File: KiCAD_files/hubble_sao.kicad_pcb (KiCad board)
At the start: 2 copper layers, 38 x 45.5 mm, 41 parts, among them J1 Conn_02x03_Counter_Clockwise, J2 Conn_02x03_Odd_Even, Q1 DMP3099L-7, SW1 SW_Push_Shielded, U1 VEML3328, U2 LSM6DSO, U3 ATmega328PB-A, U4 TLV9062xD, U5 TLV9062xD

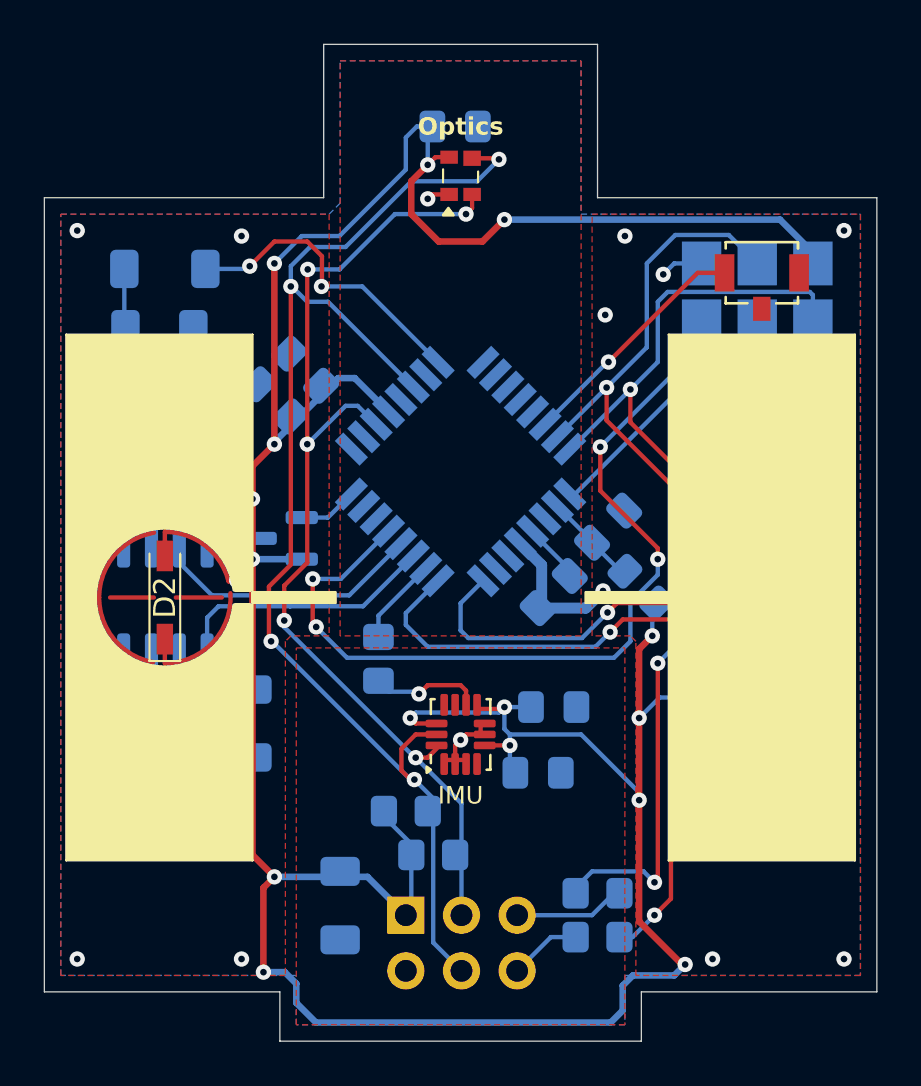
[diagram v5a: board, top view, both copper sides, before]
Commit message: Merged the front copper pours in a single ground plane
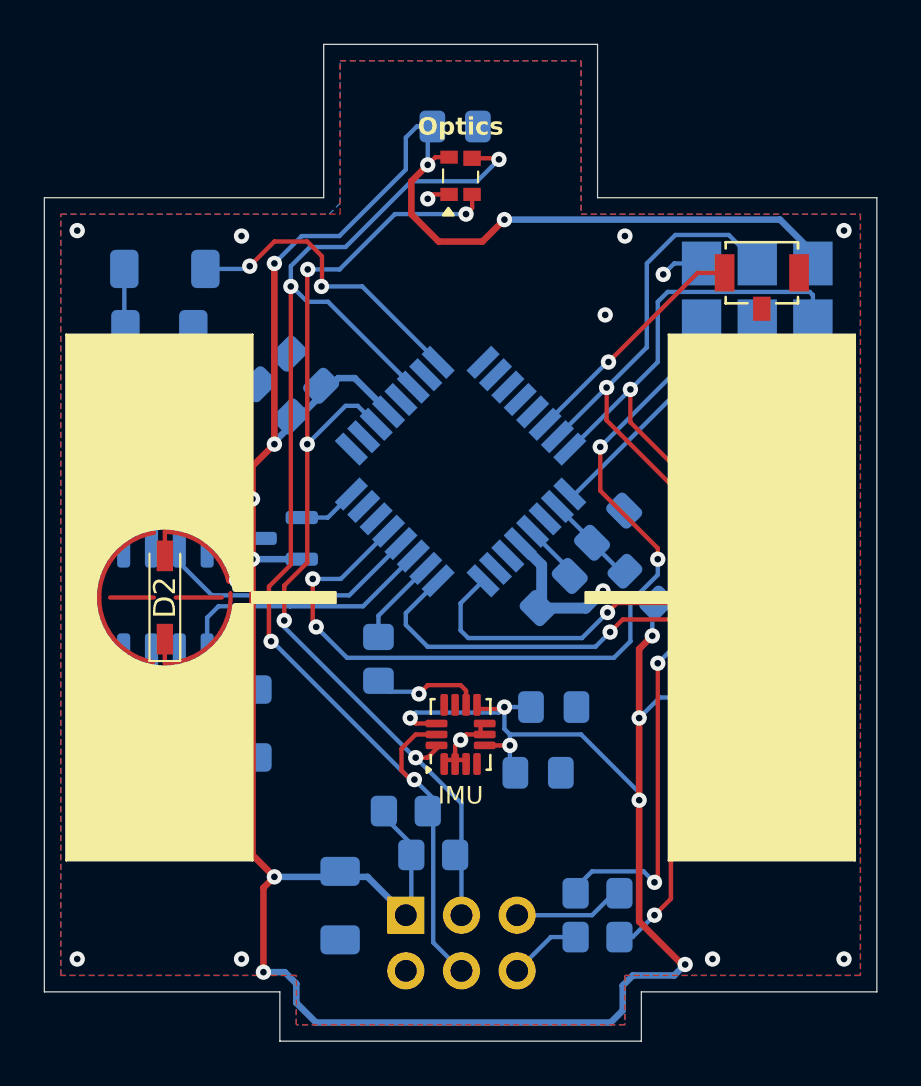
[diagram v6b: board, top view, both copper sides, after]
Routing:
- removed copper zone on F.Cu, net (none)
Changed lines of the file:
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@@
 		(tags "resistor handsolder")
 		(property "Reference" "R1"
-			(at -3.3 0 360)
+			(at -3.3 0 0)
 			(layer "B.SilkS")
 			(effects
@@
 		)
 		(property "Value" "220"
-			(at 0 -1.82 360)
+			(at 0 -1.82 0)
 			(layer "B.Fab")
 			(effects
@@
 		)
 		(fp_text user "${REFERENCE}"
-			(at -3.3 0 360)
+			(at -3.3 0 0)
 			(layer "B.Fab")
 			(effects
@@
 		(tags "diode reverse")
 		(property "Reference" "D6"
-			(at 3.75 -0.25 360)
+			(at 3.75 -0.25 0)
 			(layer "B.SilkS")
 			(effects
@@
 		)
 		(property "Value" "LED"
-			(at 0 -2.145 360)
+			(at 0 -2.145 0)
 			(layer "B.Fab")
 			(effects
@@
 		)
 		(fp_text user "${REFERENCE}"
-			(at 0 0 360)
+			(at 0 0 0)
 			(layer "B.Fab")
 			(effects
@@
 	)
 	(zone
-		(net 0)
-		(net_name "")
-		(layer "F.Cu")
-		(name "Body_panel_1")
-		(hatch edge 0.5)
-		(priority 1)
-		(connect_pads
-			(clearance 0.5)
-		)
-		(min_thickness 0.25)
-		(filled_areas_thickness no)
-		(fill yes
-			(thermal_gap 0.5)
-			(thermal_bridge_width 0.5)
-			(island_removal_mode 1)
-			(island_area_min 10)
-		)
-		(polygon
-			(pts
-				(xy 84.5 100) (xy 95.5 100) (xy 95.5 126.25) (xy 84.5 126.25)
-			)
-		)
-	)
-	(zone
-		(net 20)
-		(net_name "GND")
-		(layer "F.Cu")
-		(name "Optics_cutout")
-		(hatch edge 0.5)
-		(priority 3)
-		(connect_pads
-			(clearance 0)
-		)
-		(min_thickness 0.25)
-		(filled_areas_thickness no)
-		(fill yes
-			(thermal_gap 0.5)
-			(thermal_bridge_width 0.5)
-			(smoothing fillet)
-			(radius 0.5)
-		)
-		(polygon
-			(pts
-				(xy 71.75 107) (xy 84 107) (xy 84 126.25) (xy 82.25 126.25) (xy 82 126.5) (xy 82 141.75) (xy 71.75 141.75)
-			)
-		)
-	)
-	(zone
 		(net 20)
 		(net_name "GND")
 		(layer "F.Cu")
-		(name "Optics_cutout")
-		(hatch edge 0.5)
-		(connect_pads
-			(clearance 0)
-		)
-		(min_thickness 0.25)
-		(filled_areas_thickness no)
-		(fill yes
-			(thermal_gap 0.5)
-			(thermal_bridge_width 0.5)
-			(smoothing fillet)
-			(radius 0.5)
-		)
-		(polygon
-			(pts
-				(xy 96 107) (xy 108.25 107) (xy 108.25 141.75) (xy 98 141.75) (xy 98 126.5) (xy 97.75 126.25) (xy 96 126.25)
-			)
-		)
-	)
-	(zone
-		(net 0)
-		(net_name "")
-		(layer "F.Cu")
-		(name "Body_panel_2")
 		(hatch edge 0.5)
-		(priority 1)
 		(connect_pads
-			(clearance 0.5)
+			(clearance 0.25)
 		)
 		(min_thickness 0.25)
@@
 			(thermal_gap 0.5)
 			(thermal_bridge_width 0.5)
-			(island_removal_mode 1)
-			(island_area_min 10)
 		)
 		(polygon
 			(pts
-				(xy 82.5 126.8) (xy 97.5 126.8) (xy 97.5 144) (xy 82.5 144)
+				(xy 71.75 107) (xy 84.5 107) (xy 84.5 100) (xy 95.5 100) (xy 95.5 107) (xy 108.25 107) (xy 108.25 141.75)
+				(xy 97.5 141.75) (xy 97.5 144) (xy 82.5 144) (xy 82.5 141.75) (xy 71.75 141.75)
 			)
 		)

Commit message: Replaced some 1206 resistors by 0805s to tighten up the PCB
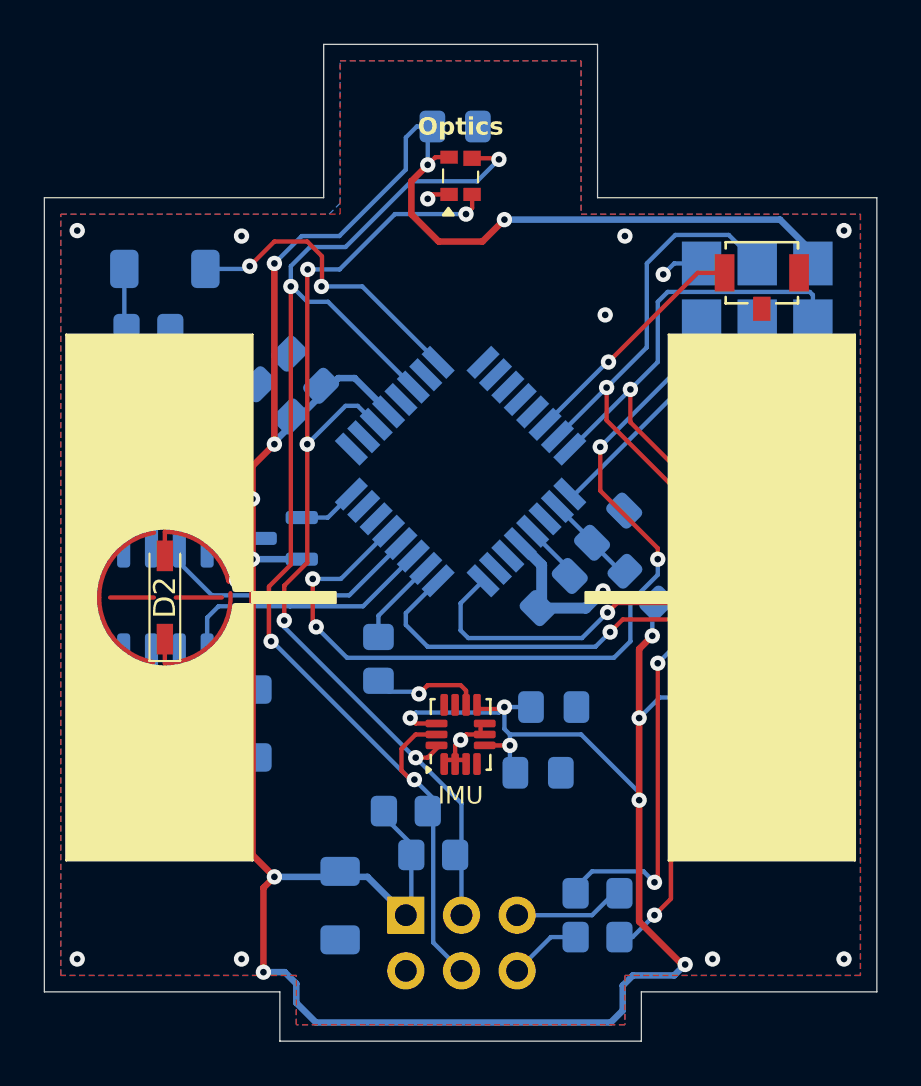
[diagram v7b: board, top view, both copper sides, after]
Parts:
- R1, R10, R3, R4, R5: footprint Resistor_SMD:R_1206_3216Metric_Pad1.30x1.75mm_HandSolder -> Resistor_SMD:R_0805_2012Metric_Pad1.20x1.40mm_HandSolder
- moved C10 1.90 mm to (77.2, 130.2)
- moved R10 1.77 mm to (77.2, 132.2)
- moved R3 1.52 mm to (103.8, 117.0)
- moved R5 1.52 mm to (75.8, 117.0)
- moved R4 1.37 mm to (104.5, 132.2)
- moved C14 1.27 mm to (75.8, 119.2)
- moved C8 1.25 mm to (103.8, 119.0)
- moved C9 1.00 mm to (104.5, 130.0)
- moved R1 0.50 mm to (75.8, 112.2)
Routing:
- net Net-(D1-K): track 11.6 -> 8.46 mm
- net Net-(D3-K): track 12.1 -> 8.91 mm
- net Net-(D5-K): track 10.8 -> 7.87 mm
- net Net-(D4-K): track 12.0 -> 9.09 mm
- net /PANEL3: track 25.2 -> 23.0 mm
- net /PANEL2: track 19.0 -> 17.0 mm
- net /PANEL4: track 27.6 -> 26.0 mm
- net /PANEL1: track 19.0 -> 17.5 mm

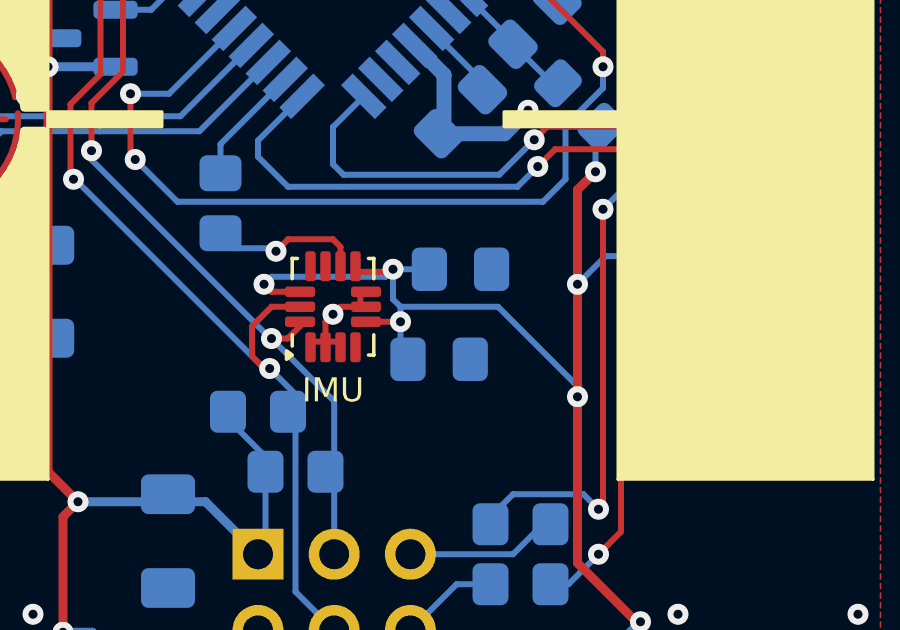
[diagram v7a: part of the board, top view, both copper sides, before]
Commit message: Cleaned up the PCB around the IMU
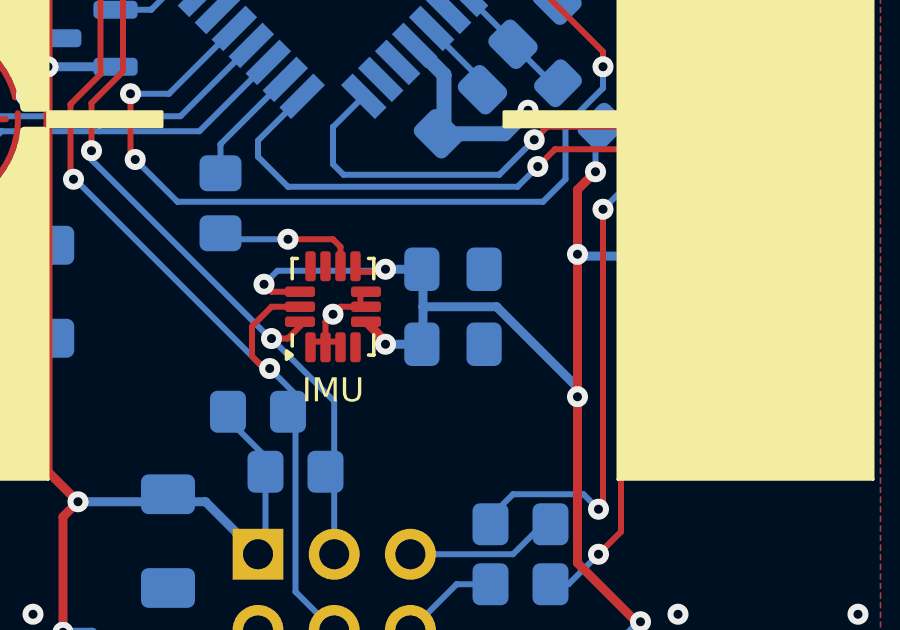
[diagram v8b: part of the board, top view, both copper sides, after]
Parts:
- moved C3 0.68 mm to (94.0, 132.0)
- moved C5 0.25 mm to (94.0, 129.5)
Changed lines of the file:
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@@
 	(footprint "Capacitor_SMD:C_0805_2012Metric_Pad1.18x1.45mm_HandSolder"
 		(layer "B.Cu")
-		(at 93.5375 132.5)
+		(at 94 132)
 		(descr "Capacitor SMD 0805 (2012 Metric), square (rectangular) end terminal, IPC_7351 nominal with elongated pad for handsoldering. (Body size source: IPC-SM-782 page 76, https://www.pcb-3d.com/wordpress/wp-content/uploads/ipc-sm-782a_amendment_1_and_2.pdf, https://docs.google.com/spreadsheets/d/1BsfQQcO9C6DZCsRaXUlFlo91Tg2WpOkGARC1WS5S8t0/edit?usp=sharing), generated with kicad-footprint-generator")
 		(tags "capacitor handsolder")
@@
 	(footprint "Capacitor_SMD:C_0805_2012Metric_Pad1.18x1.45mm_HandSolder"
 		(layer "B.Cu")
-		(at 94.25 129.5)
+		(at 94 129.5)
 		(descr "Capacitor SMD 0805 (2012 Metric), square (rectangular) end terminal, IPC_7351 nominal with elongated pad for handsoldering. (Body size source: IPC-SM-782 page 76, https://www.pcb-3d.com/wordpress/wp-content/uploads/ipc-sm-782a_amendment_1_and_2.pdf, https://docs.google.com/spreadsheets/d/1BsfQQcO9C6DZCsRaXUlFlo91Tg2WpOkGARC1WS5S8t0/edit?usp=sharing), generated with kicad-footprint-generator")
 		(tags "capacitor handsolder")
@@
 	)
 	(segment
-		(start 92.25 131.25)
-		(end 91.1 131.25)
-		(width 0.2)
-		(layer "F.Cu")
-		(net 18)
-	)
-	(segment
 		(start 81.5 137.25)
 		(end 80.5 136.25)
@@
 	)
 	(segment
-		(start 92 129.5)
-		(end 91.9125 129.5875)
-		(width 0.2)
-		(layer "F.Cu")
-		(net 18)
-	)
-	(segment
 		(start 81 137.75)
 		(end 81.5 137.25)
@@
 	)
 	(segment
-		(start 87.75 105.5)
-		(end 88.5 104.75)
+		(start 91.75 132)
+		(end 91.75 131.9)
 		(width 0.3)
 		(layer "F.Cu")
@@
 	)
 	(segment
-		(start 91.9125 129.5875)
-		(end 90.75 129.5875)
-		(width 0.2)
+		(start 91.75 131.9)
+		(end 91.1 131.25)
+		(width 0.3)
+		(layer "F.Cu")
+		(net 18)
+	)
+	(segment
+		(start 87.75 105.5)
+		(end 88.5 104.75)
+		(width 0.3)
 		(layer "F.Cu")
 		(net 18)
@@
 	)
 	(segment
+		(start 91.75 129.5)
+		(end 91.6625 129.5875)
+		(width 0.2)
+		(layer "F.Cu")
+		(net 18)
+	)
+	(segment
 		(start 87.75 107)
 		(end 87.75 105.5)
@@
 	)
 	(segment
+		(start 91.6625 129.5875)
+		(end 90.75 129.5875)
+		(width 0.2)
+		(layer "F.Cu")
+		(net 18)
+	)
+	(segment
 		(start 80.5 118.5)
 		(end 81.5 117.5)
@@
 	)
 	(via
-		(at 92.25 131.25)
-		(size 0.7)
-		(drill 0.3)
-		(layers "F.Cu" "B.Cu")
-		(net 18)
-	)
-	(via
 		(at 80.5 122.75)
 		(size 0.7)
@@
 	)
 	(via
-		(at 98.15 130)
+		(at 98.15 129)
 		(size 0.7)
 		(drill 0.3)
@@
 	)
 	(via
-		(at 92 129.5)
+		(at 91.75 129.5)
 		(size 0.7)
 		(drill 0.3)
@@
 		(net 18)
 	)
-	(segment
-		(start 92.25 131.25)
-		(end 92.25 132)
-		(width 0.2)
-		(layer "B.Cu")
+	(via
+		(at 91.75 132)
+		(size 0.7)
+		(drill 0.3)
+		(layers "F.Cu" "B.Cu")
 		(net 18)
 	)
@@
 	)
 	(segment
+		(start 93 130.75)
+		(end 93 129.5375)
+		(width 0.3)
+		(layer "B.Cu")
+		(net 18)
+	)
+	(segment
 		(start 81.5 117.401471)
 		(end 84.417848 114.483623)
@@
 	)
 	(segment
+		(start 92.6375 129.575)
+		(end 92.7125 129.5)
+		(width 0.2)
+		(layer "B.Cu")
+		(net 18)
+	)
+	(segment
 		(start 87.5 103.5)
 		(end 88 103)
@@
 	)
 	(segment
-		(start 98.15 133.75)
-		(end 98.15 133.4)
+		(start 91.7 129.55)
+		(end 88.15 129.55)
 		(width 0.2)
 		(layer "B.Cu")
@@
 	)
 	(segment
-		(start 99.0875 129.0625)
-		(end 101.5 129.0625)
-		(width 0.2)
+		(start 93 130.75)
+		(end 93 131.9625)
+		(width 0.3)
 		(layer "B.Cu")
 		(net 18)
@@
 	)
 	(segment
+		(start 88.15 129.55)
+		(end 87.7 130)
+		(width 0.2)
+		(layer "B.Cu")
+		(net 18)
+	)
+	(segment
 		(start 88.5 103.2125)
 		(end 88.5 104.75)
@@
 	)
 	(segment
+		(start 92.9625 132)
+		(end 91.75 132)
+		(width 0.3)
+		(layer "B.Cu")
+		(net 18)
+	)
+	(segment
 		(start 81.975 141.6)
 		(end 82.5 142.125)
@@
 	)
 	(segment
-		(start 92.25 131.25)
-		(end 92.25 130.75)
+		(start 91.75 129.5)
+		(end 91.7 129.55)
 		(width 0.2)
 		(layer "B.Cu")
@@
 	)
 	(segment
-		(start 83.4 143.9)
-		(end 96.85 143.9)
+		(start 91.75 129.5)
+		(end 92.9625 129.5)
 		(width 0.3)
 		(layer "B.Cu")
@@
 	)
 	(segment
-		(start 91.75 129.75)
-		(end 92 129.5)
-		(width 0.2)
+		(start 93 129.5375)
+		(end 92.9625 129.5)
+		(width 0.3)
 		(layer "B.Cu")
 		(net 18)
 	)
 	(segment
-		(start 98.15 133.4)
-		(end 95.5 130.75)
-		(width 0.2)
+		(start 83.4 143.9)
+		(end 96.85 143.9)
+		(width 0.3)
 		(layer "B.Cu")
 		(net 18)
 	)
 	(segment
-		(start 85.167937 114.483623)
-		(end 86.711953 116.027639)
+		(start 98.15 129)
+		(end 98.2125 129.0625)
 		(width 0.3)
 		(layer "B.Cu")
@@
 	)
 	(segment
-		(start 98.15 130)
-		(end 99.0875 129.0625)
-		(width 0.2)
+		(start 85.167937 114.483623)
+		(end 86.711953 116.027639)
+		(width 0.3)
 		(layer "B.Cu")
 		(net 18)
@@
 	)
 	(segment
-		(start 92 130.5)
-		(end 92.25 130.75)
-		(width 0.2)
-		(layer "B.Cu")
-		(net 18)
-	)
-	(segment
 		(start 82.75 108)
 		(end 84.467157 108)
@@
 	)
 	(segment
-		(start 92 129.5)
-		(end 92.7125 129.5)
-		(width 0.2)
-		(layer "B.Cu")
-		(net 18)
-	)
-	(segment
 		(start 81.5 117.5)
 		(end 81.5 117.401471)
@@
 	)
 	(segment
-		(start 92 129.5)
-		(end 92 130.5)
-		(width 0.2)
-		(layer "B.Cu")
-		(net 18)
-	)
-	(segment
-		(start 95.5 130.75)
-		(end 92.25 130.75)
-		(width 0.2)
-		(layer "B.Cu")
-		(net 18)
-	)
-	(segment
 		(start 86.25 134.25)
 		(end 87.75 135.75)
@@
 	)
 	(segment
-		(start 87.95 129.75)
-		(end 91.75 129.75)
-		(width 0.2)
+		(start 93 131.9625)
+		(end 92.9625 132)
+		(width 0.3)
+		(layer "B.Cu")
+		(net 18)
+	)
+	(segment
+		(start 98.15 133.75)
+		(end 98.15 133.444544)
+		(width 0.3)
 		(layer "B.Cu")
 		(net 18)
@@
 	)
 	(segment
-		(start 87.7 130)
-		(end 87.95 129.75)
-		(width 0.2)
+		(start 98.15 133.444544)
+		(end 95.455456 130.75)
+		(width 0.3)
+		(layer "B.Cu")
+		(net 18)
+	)
+	(segment
+		(start 95.455456 130.75)
+		(end 93 130.75)
+		(width 0.3)
+		(layer "B.Cu")
+		(net 18)
+	)
+	(segment
+		(start 98.2125 129.0625)
+		(end 101.5 129.0625)
+		(width 0.3)
 		(layer "B.Cu")
 		(net 18)
@@
 	)
 	(segment
-		(start 88.1 128.9)
-		(end 88.5 128.5)
-		(width 0.2)
-		(layer "F.Cu")
-		(net 32)
-	)
-	(segment
-		(start 90 128.5)
-		(end 90.25 128.75)
+		(start 90.25 128.75)
+		(end 90.25 129.4)
 		(width 0.2)
 		(layer "F.Cu")
@@
 	)
 	(segment
-		(start 90.25 128.75)
-		(end 90.25 129.4)
+		(start 90 128.5)
+		(end 90.25 128.75)
 		(width 0.2)
 		(layer "F.Cu")
@@
 	)
 	(via
-		(at 88.1 128.9)
+		(at 88.5 128.5)
 		(size 0.7)
 		(drill 0.3)
@@
 	)
 	(segment
-		(start 88 128.8)
-		(end 86.75 128.8)
+		(start 88.5 128.5)
+		(end 86.45 128.5)
 		(width 0.2)
 		(layer "B.Cu")
@@
 	)
 	(segment
-		(start 86.75 128.8)
+		(start 86.45 128.5)
 		(end 86.25 128.3)
 		(width 0.2)
 		(layer "B.Cu")
-		(net 32)
-	)
-	(segment
-		(start 88.1 128.9)
-		(end 88 128.8)
-		(width 0.2)
-		(layer "B.Cu")
